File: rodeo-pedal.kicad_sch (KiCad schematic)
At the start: 20 parts, among them J1 USB_C_Receptacle_USB2.0, U1 STM32F205RETx, Y1 16MHz

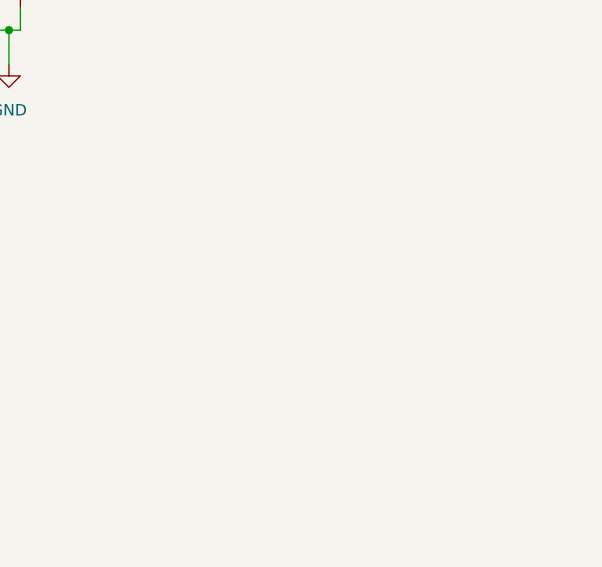
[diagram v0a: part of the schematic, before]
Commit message: Add LDO regulator
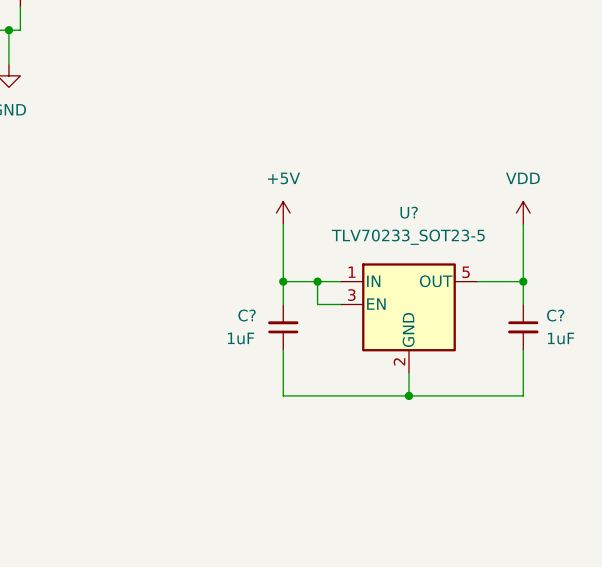
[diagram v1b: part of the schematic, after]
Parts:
- added C? (x2): 1uF, symbol Device:C_Small
- added U?: TLV70233_SOT23-5, Package_TO_SOT_SMD:SOT-23-5, symbol Regulator_Linear:TLV70233_SOT23-5
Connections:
- net +5V: now also C?.2, U?.1 (IN), U?.3 (EN)
- net VDD: now also C?.1, U?.5 (OUT)
- new net: C?.1, C?.2, U?.2 (GND)
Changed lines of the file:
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@@
   (junction (at 77.47 49.53) (diameter 0) (color 0 0 0 0)
   )
+  (junction (at 248.92 102.87) (diameter 0) (color 0 0 0 0)
+  )
   (junction (at 129.54 69.85) (diameter 0) (color 0 0 0 0)
   )
@@
   (junction (at 151.13 48.26) (diameter 0) (color 0 0 0 0)
   )
+  (junction (at 234.95 90.17) (diameter 0) (color 0 0 0 0)
+  )
   (junction (at 76.2 147.32) (diameter 0) (color 0 0 0 0)
   )
@@
   (junction (at 45.72 69.85) (diameter 0) (color 0 0 0 0)
   )
+  (junction (at 261.62 90.17) (diameter 0) (color 0 0 0 0)
+  )
   (junction (at 67.31 30.48) (diameter 0) (color 0 0 0 0)
+  )
+  (junction (at 238.76 90.17) (diameter 0) (color 0 0 0 0)
   )
   (junction (at 62.23 43.18) (diameter 0) (color 0 0 0 0)
@@
     (stroke (width 0) (type default) (color 0 0 0 0))
   )
+  (wire (pts (xy 238.76 90.17) (xy 241.3 90.17))
+    (stroke (width 0) (type default) (color 0 0 0 0))
+  )
   (wire (pts (xy 78.74 49.53) (xy 77.47 49.53))
     (stroke (width 0) (type default) (color 0 0 0 0))
@@
     (stroke (width 0) (type default) (color 0 0 0 0))
   )
+  (wire (pts (xy 261.62 92.71) (xy 261.62 90.17))
+    (stroke (width 0) (type default) (color 0 0 0 0))
+  )
   (wire (pts (xy 93.98 85.09) (xy 96.52 85.09))
     (stroke (width 0) (type default) (color 0 0 0 0))
@@
     (stroke (width 0) (type default) (color 0 0 0 0))
   )
+  (wire (pts (xy 234.95 102.87) (xy 248.92 102.87))
+    (stroke (width 0) (type default) (color 0 0 0 0))
+  )
   (wire (pts (xy 148.59 41.91) (xy 151.13 41.91))
     (stroke (width 0) (type default) (color 0 0 0 0))
@@
     (stroke (width 0) (type default) (color 0 0 0 0))
   )
+  (wire (pts (xy 261.62 83.82) (xy 261.62 90.17))
+    (stroke (width 0) (type default) (color 0 0 0 0))
+  )
   (wire (pts (xy 151.13 46.99) (xy 151.13 48.26))
     (stroke (width 0) (type default) (color 0 0 0 0))
@@
     (stroke (width 0) (type default) (color 0 0 0 0))
   )
+  (wire (pts (xy 241.3 92.71) (xy 238.76 92.71))
+    (stroke (width 0) (type default) (color 0 0 0 0))
+  )
   (wire (pts (xy 43.18 83.82) (xy 43.18 87.63))
     (stroke (width 0) (type default) (color 0 0 0 0))
   )
+  (wire (pts (xy 234.95 92.71) (xy 234.95 90.17))
+    (stroke (width 0) (type default) (color 0 0 0 0))
+  )
   (wire (pts (xy 151.13 48.26) (xy 151.13 49.53))
     (stroke (width 0) (type default) (color 0 0 0 0))
@@
     (stroke (width 0) (type default) (color 0 0 0 0))
   )
+  (wire (pts (xy 234.95 90.17) (xy 238.76 90.17))
+    (stroke (width 0) (type default) (color 0 0 0 0))
+  )
   (wire (pts (xy 36.83 99.06) (xy 36.83 100.33))
     (stroke (width 0) (type default) (color 0 0 0 0))
@@
     (stroke (width 0) (type default) (color 0 0 0 0))
   )
+  (wire (pts (xy 234.95 83.82) (xy 234.95 90.17))
+    (stroke (width 0) (type default) (color 0 0 0 0))
+  )
   (wire (pts (xy 151.13 48.26) (xy 153.67 48.26))
     (stroke (width 0) (type default) (color 0 0 0 0))
@@
     (stroke (width 0) (type default) (color 0 0 0 0))
   )
+  (wire (pts (xy 261.62 97.79) (xy 261.62 102.87))
+    (stroke (width 0) (type default) (color 0 0 0 0))
+  )
   (wire (pts (xy 73.66 143.51) (xy 73.66 147.32))
     (stroke (width 0) (type default) (color 0 0 0 0))
@@
     (stroke (width 0) (type default) (color 0 0 0 0))
   )
+  (wire (pts (xy 234.95 97.79) (xy 234.95 102.87))
+    (stroke (width 0) (type default) (color 0 0 0 0))
+  )
   (wire (pts (xy 67.31 36.83) (xy 67.31 43.18))
     (stroke (width 0) (type default) (color 0 0 0 0))
@@
     (stroke (width 0) (type default) (color 0 0 0 0))
   )
+  (wire (pts (xy 238.76 92.71) (xy 238.76 90.17))
+    (stroke (width 0) (type default) (color 0 0 0 0))
+  )
   (wire (pts (xy 91.44 26.67) (xy 91.44 27.94))
     (stroke (width 0) (type default) (color 0 0 0 0))
@@
     (stroke (width 0) (type default) (color 0 0 0 0))
   )
+  (wire (pts (xy 261.62 102.87) (xy 248.92 102.87))
+    (stroke (width 0) (type default) (color 0 0 0 0))
+  )
   (wire (pts (xy 93.98 120.65) (xy 107.95 120.65))
     (stroke (width 0) (type default) (color 0 0 0 0))
@@
   )
   (wire (pts (xy 151.13 35.56) (xy 151.13 34.29))
+    (stroke (width 0) (type default) (color 0 0 0 0))
+  )
+  (wire (pts (xy 261.62 90.17) (xy 256.54 90.17))
+    (stroke (width 0) (type default) (color 0 0 0 0))
+  )
+  (wire (pts (xy 248.92 102.87) (xy 248.92 100.33))
     (stroke (width 0) (type default) (color 0 0 0 0))
   )
@@
     (pin "1")
   )
+  (symbol (lib_id "Regulator_Linear:TLV70233_SOT23-5") (at 248.92 92.71 0) (unit 1)
+    (in_bom yes) (on_board yes) (fields_autoplaced)
+    (property "Reference" "U?" (id 0) (at 248.92 82.55 0))
+    (property "Value" "TLV70233_SOT23-5" (id 1) (at 248.92 85.09 0))
+    (property "Footprint" "Package_TO_SOT_SMD:SOT-23-5" (id 2) (at 248.92 84.455 0)
+      (effects (font (size 1.27 1.27) italic) hide)
+    )
+    (property "Datasheet" "http://www.ti.com/lit/ds/symlink/tlv702.pdf" (id 3) (at 248.92 91.44 0)
+      (effects (font (size 1.27 1.27)) hide)
+    )
+    (pin "1")
+    (pin "2")
+    (pin "3")
+    (pin "4")
+    (pin "5")
+  )
   (symbol (lib_id "Device:C_Small") (at 69.85 38.1 0) (unit 1)
     (in_bom yes) (on_board yes)
@@
     (pin "2")
   )
+  (symbol (lib_id "Device:C_Small") (at 261.62 95.25 0) (unit 1)
+    (in_bom yes) (on_board yes) (fields_autoplaced)
+    (property "Reference" "C?" (id 0) (at 264.16 93.9862 0)
+      (effects (font (size 1.27 1.27)) (justify left))
+    )
+    (property "Value" "1uF" (id 1) (at 264.16 96.5262 0)
+      (effects (font (size 1.27 1.27)) (justify left))
+    )
+    (property "Footprint" "" (id 2) (at 261.62 95.25 0)
+      (effects (font (size 1.27 1.27)) hide)
+    )
+    (property "Datasheet" "~" (id 3) (at 261.62 95.25 0)
+      (effects (font (size 1.27 1.27)) hide)
+    )
+    (pin "1")
+    (pin "2")
+  )
   (symbol (lib_id "power:GND") (at 76.2 149.86 0) (unit 1)
     (in_bom yes) (on_board yes)
@@
     )
     (property "Datasheet" "" (id 3) (at 76.2 149.86 0)
+      (effects (font (size 1.27 1.27)) hide)
+    )
+    (pin "1")
+  )
+  (symbol (lib_id "power:VDD") (at 261.62 83.82 0) (unit 1)
+    (in_bom yes) (on_board yes) (fields_autoplaced)
+    (property "Reference" "#PWR?" (id 0) (at 261.62 87.63 0)
+      (effects (font (size 1.27 1.27)) hide)
+    )
+    (property "Value" "VDD" (id 1) (at 261.62 78.74 0))
+    (property "Footprint" "" (id 2) (at 261.62 83.82 0)
+      (effects (font (size 1.27 1.27)) hide)
+    )
+    (property "Datasheet" "" (id 3) (at 261.62 83.82 0)
       (effects (font (size 1.27 1.27)) hide)
     )
@@
     (pin "2")
   )
+  (symbol (lib_id "Device:C_Small") (at 234.95 95.25 180) (unit 1)
+    (in_bom yes) (on_board yes)
+    (property "Reference" "C?" (id 0) (at 229.87 93.98 0)
+      (effects (font (size 1.27 1.27)) (justify right))
+    )
+    (property "Value" "1uF" (id 1) (at 228.6 96.52 0)
+      (effects (font (size 1.27 1.27)) (justify right))
+    )
+    (property "Footprint" "" (id 2) (at 234.95 95.25 0)
+      (effects (font (size 1.27 1.27)) hide)
+    )
+    (property "Datasheet" "~" (id 3) (at 234.95 95.25 0)
+      (effects (font (size 1.27 1.27)) hide)
+    )
+    (pin "1")
+    (pin "2")
+  )
   (symbol (lib_id "Device:C_Small") (at 49.53 67.31 270) (unit 1)
     (in_bom yes) (on_board yes)
@@
     (pin "1")
   )
+  (symbol (lib_id "power:+5V") (at 234.95 83.82 0) (unit 1)
+    (in_bom yes) (on_board yes) (fields_autoplaced)
+    (property "Reference" "#PWR?" (id 0) (at 234.95 87.63 0)
+      (effects (font (size 1.27 1.27)) hide)
+    )
+    (property "Value" "+5V" (id 1) (at 234.95 78.74 0))
+    (property "Footprint" "" (id 2) (at 234.95 83.82 0)
+      (effects (font (size 1.27 1.27)) hide)
+    )
+    (property "Datasheet" "" (id 3) (at 234.95 83.82 0)
+      (effects (font (size 1.27 1.27)) hide)
+    )
+    (pin "1")
+  )
   (symbol (lib_id "Device:R_Small") (at 157.48 35.56 90) (unit 1)
     (in_bom yes) (on_board yes)
@@
       (reference "#PWR?") (unit 1) (value "GND") (footprint "")
     )
+    (path "/6c4108f1-2c47-4829-a85f-5e6fd24b5e31"
+      (reference "#PWR?") (unit 1) (value "VDD") (footprint "")
+    )
     (path "/71dc3b26-3edc-4aa8-8c53-86d765314045"
       (reference "#PWR?") (unit 1) (value "+5V") (footprint "")
@@
       (reference "#PWR?") (unit 1) (value "GND") (footprint "")
     )
+    (path "/ee28ddc6-930e-45e2-889f-ca2e620ceaa7"
+      (reference "#PWR?") (unit 1) (value "+5V") (footprint "")
+    )
     (path "/fc1265ce-588f-49eb-8184-96c738cbad8a"
       (reference "#PWR?") (unit 1) (value "VDD") (footprint "")
@@
       (reference "C13") (unit 1) (value "100nF") (footprint "")
     )
+    (path "/605f7ed9-4fa9-43fa-b616-75155724a50e"
+      (reference "C?") (unit 1) (value "1uF") (footprint "")
+    )
+    (path "/a7dcbdb1-4525-4b96-9275-982ce6c15f1c"
+      (reference "C?") (unit 1) (value "1uF") (footprint "")
+    )
     (path "/6d29d722-60e8-4e56-91cf-ecdafe1686bf"
       (reference "D?") (unit 1) (value "LED") (footprint "")
@@
       (reference "U?") (unit 1) (value "TJA1042TK-3") (footprint "Package_DFN_QFN:DFN-8-1EP_3x3mm_P0.65mm_EP1.55x2.4mm")
     )
+    (path "/46bac8d3-7a7f-42ac-8981-f0a12a311337"
+      (reference "U?") (unit 1) (value "TLV70233_SOT23-5") (footprint "Package_TO_SOT_SMD:SOT-23-5")
+    )
     (path "/b1f834e9-059b-49d8-a9ca-92d35cc098d6"
